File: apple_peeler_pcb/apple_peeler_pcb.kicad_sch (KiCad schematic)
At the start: 14 parts, among them J1 BM03B-SRSS-TB, J2 BM03B-SRSS-TB, SW1 SPST BTN, SW2 SPST BTN, U1 W25Q16JVSS, U2 RP2040, Y1 12MHz

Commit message: use wleds instead of individual leds
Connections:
- net UI/GREEN_LED renamed UI/WLED
- net UI/RED_LED: no longer names the net of U2.7 (GPIO5)
- net UI/YELLOW_LED: no longer names the net of U2.8 (GPIO6)
- no-connect marks 8 -> 10
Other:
- sheet UI ports: added WLED; removed GREEN_LED, RED_LED, YELLOW_LED
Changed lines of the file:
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@@
 	)
 	(no_connect
+		(at 168.91 88.9)
+	)
+	(no_connect
+		(at 168.91 91.44)
+	)
+	(no_connect
 		(at 168.91 144.78)
 	)
@@
 	(wire
 		(pts
-			(xy 168.91 91.44) (xy 181.61 91.44)
-		)
-		(stroke
-			(width 0)
-			(type default)
-		)
-	)
-	(wire
-		(pts
 			(xy 80.01 96.52) (xy 101.6 96.52)
 		)
@@
 	(wire
 		(pts
-			(xy 168.91 88.9) (xy 181.61 88.9)
-		)
-		(stroke
-			(width 0)
-			(type default)
-		)
-	)
-	(wire
-		(pts
 			(xy 87.63 91.44) (xy 87.63 93.98)
 		)
@@
 	(sheet
 		(at 181.61 82.55)
-		(size 17.78 10.16)
+		(size 17.78 5.08)
 		(exclude_from_sim no)
 		(in_bom yes)
@@
 		)
 		(property "Sheetfile" "ui.kicad_sch"
-			(at 181.61 93.2946 0)
+			(at 181.61 88.2146 0)
 			(effects
 				(font
@@
 			)
 		)
-		(pin "GREEN_LED" input
-			(at 181.61 86.36 180)
-			(effects
-				(font
-					(size 1.27 1.27)
-				)
-				(justify left)
-			)
-		)
-		(pin "RED_LED" input
-			(at 181.61 88.9 180)
-			(effects
-				(font
-					(size 1.27 1.27)
-				)
-				(justify left)
-			)
-		)
 		(pin "USR_BTN" output
 			(at 181.61 83.82 180)
@@
 			)
 		)
-		(pin "YELLOW_LED" input
-			(at 181.61 91.44 180)
+		(pin "WLED" input
+			(at 181.61 86.36 180)
 			(effects
 				(font

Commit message: some progress
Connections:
- net USB/DM renamed USB/DN
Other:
- sheet USB ports: added DN; removed DM
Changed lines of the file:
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@@
 			)
 		)
-		(pin "DM" bidirectional
+		(pin "DN" bidirectional
 			(at 115.57 86.36 0)
 			(effects

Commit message: rg | xargs sed goes brrr
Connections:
- net HDMI passthrough/CEC_SINK_MON renamed HDMI passthrough/CEC_B_MON
- net HDMI passthrough/CEC_SINK_PULLDOWN renamed HDMI passthrough/CEC_B_PULLDOWN
- net HDMI passthrough/CEC_SRC_MON renamed HDMI passthrough/CEC_A_MON
- net HDMI passthrough/CEC_SRC_PULLDOWN renamed HDMI passthrough/CEC_A_PULLDOWN
- net HDMI passthrough/HPD_SINK_ASSERT renamed HDMI passthrough/HPD_B_ASSERT
- net HDMI passthrough/HPD_SINK_MON renamed HDMI passthrough/HPD_B_MON
- net HDMI passthrough/HPD_SRC_ASSERT renamed HDMI passthrough/HPD_A_ASSERT
- net HDMI passthrough/HPD_SRC_MON renamed HDMI passthrough/HPD_A_MON
- net HDMI passthrough/SCL_SINK_3V3 renamed HDMI passthrough/SCL_B_3V3
- net HDMI passthrough/SCL_SRC_3V3 renamed HDMI passthrough/SCL_A_3V3
- net HDMI passthrough/SDA_SINK_3V3 renamed HDMI passthrough/SDA_B_3V3
- net HDMI passthrough/SDA_SRC_3V3 renamed HDMI passthrough/SDA_A_3V3
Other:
- sheet HDMI passthrough ports: added CEC_A_MON, CEC_A_PULLDOWN, CEC_B_MON, CEC_B_PULLDOWN, HPD_A_ASSERT, HPD_A_MON, HPD_B_ASSERT, HPD_B_MON, SCL_A_3V3, SCL_B_3V3, SDA_A_3V3, SDA_B_3V3; removed CEC_SINK_MON, CEC_SINK_PULLDOWN, CEC_SRC_MON, CEC_SRC_PULLDOWN, HPD_SINK_ASSERT, HPD_SINK_MON, HPD_SRC_ASSERT, HPD_SRC_MON, SCL_SINK_3V3, SCL_SRC_3V3, SDA_SINK_3V3, SDA_SRC_3V3
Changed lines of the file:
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@@
 			)
 		)
-		(pin "HPD_SINK_MON" output
+		(pin "HPD_B_MON" output
 			(at 228.6 121.92 180)
 			(effects
@@
 			)
 		)
-		(pin "HPD_SRC_ASSERT" input
+		(pin "HPD_A_ASSERT" input
 			(at 228.6 119.38 180)
 			(effects
@@
 			)
 		)
-		(pin "SCL_SINK_3V3" bidirectional
+		(pin "SCL_B_3V3" bidirectional
 			(at 228.6 109.22 180)
 			(effects
@@
 			)
 		)
-		(pin "SCL_SRC_3V3" bidirectional
+		(pin "SCL_A_3V3" bidirectional
 			(at 228.6 104.14 180)
 			(effects
@@
 			)
 		)
-		(pin "SDA_SINK_3V3" bidirectional
+		(pin "SDA_B_3V3" bidirectional
 			(at 228.6 106.68 180)
 			(effects
@@
 			)
 		)
-		(pin "SDA_SRC_3V3" bidirectional
+		(pin "SDA_A_3V3" bidirectional
 			(at 228.6 101.6 180)
 			(effects
@@
 			)
 		)
-		(pin "CEC_SINK_MON" output
+		(pin "CEC_B_MON" output
 			(at 228.6 129.54 180)
 			(effects
@@
 			)
 		)
-		(pin "CEC_SINK_PULLDOWN" input
+		(pin "CEC_B_PULLDOWN" input
 			(at 228.6 132.08 180)
 			(effects
@@
 			)
 		)
-		(pin "CEC_SRC_MON" output
+		(pin "CEC_A_MON" output
 			(at 228.6 137.16 180)
 			(effects
@@
 			)
 		)
-		(pin "CEC_SRC_PULLDOWN" input
+		(pin "CEC_A_PULLDOWN" input
 			(at 228.6 134.62 180)
 			(effects
@@
 			)
 		)
-		(pin "HPD_SINK_ASSERT" input
+		(pin "HPD_B_ASSERT" input
 			(at 228.6 124.46 180)
 			(effects
@@
 			)
 		)
-		(pin "HPD_SRC_MON" output
+		(pin "HPD_A_MON" output
 			(at 228.6 116.84 180)
 			(effects

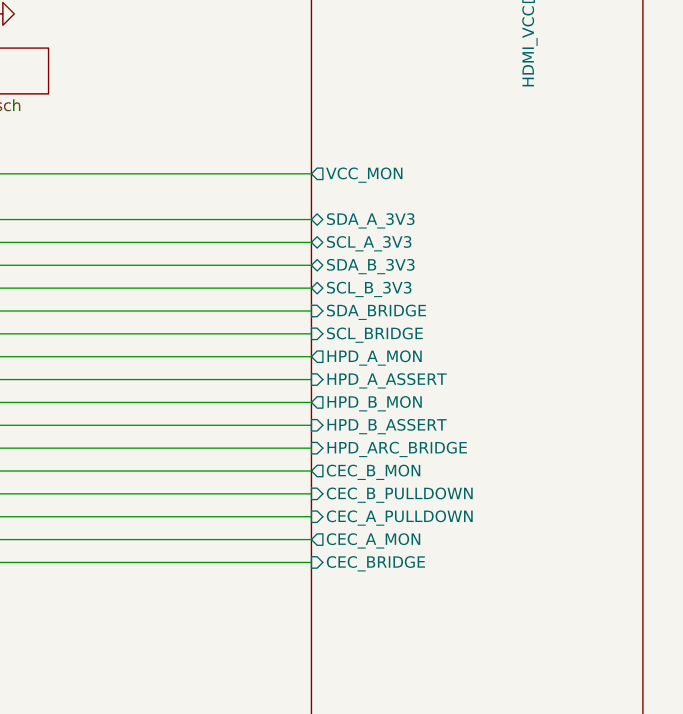
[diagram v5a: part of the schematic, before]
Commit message: route all the rp2040 pins
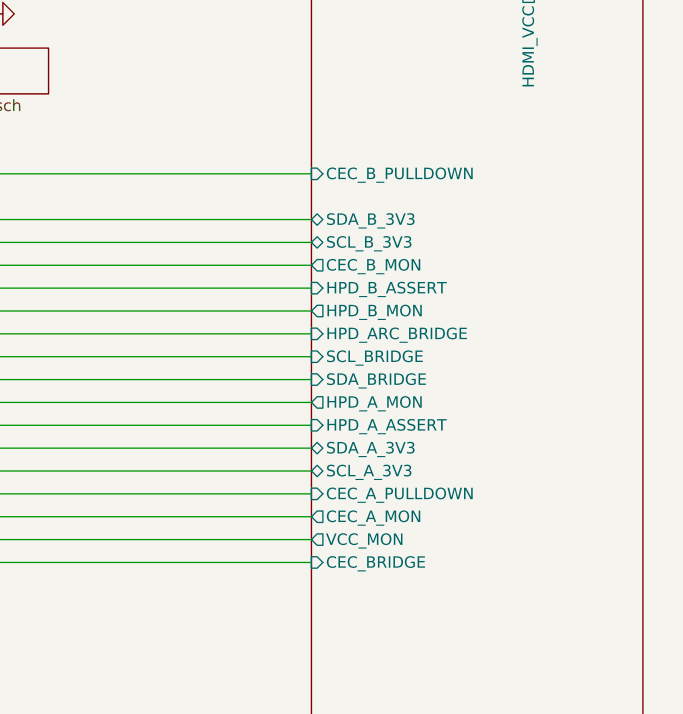
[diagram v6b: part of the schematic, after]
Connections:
- net HDMI passthrough/CEC_A_MON: now also U2.35 (GPIO23); no longer U2.36 (GPIO24)
- net HDMI passthrough/CEC_A_PULLDOWN: now also U2.34 (GPIO22); no longer U2.35 (GPIO23)
- net HDMI passthrough/CEC_B_MON: now also U2.15 (GPIO12); no longer U2.32 (GPIO21)
- net HDMI passthrough/CEC_B_PULLDOWN: now also U2.11 (GPIO8); no longer U2.34 (GPIO22)
- net HDMI passthrough/HPD_ARC_BRIDGE: now also U2.18 (GPIO15); no longer U2.31 (GPIO20)
- net HDMI passthrough/HPD_A_ASSERT: now also U2.30 (GPIO19); no longer U2.28 (GPIO17)
- net HDMI passthrough/HPD_A_MON: now also U2.29 (GPIO18); no longer U2.27 (GPIO16)
- net HDMI passthrough/HPD_B_ASSERT: now also U2.16 (GPIO13); no longer U2.30 (GPIO19)
- net HDMI passthrough/HPD_B_MON: now also U2.17 (GPIO14); no longer U2.29 (GPIO18)
- net HDMI passthrough/SCL_A_3V3: now also U2.32 (GPIO21); no longer U2.14 (GPIO11)
- net HDMI passthrough/SCL_BRIDGE: now also U2.27 (GPIO16); no longer U2.18 (GPIO15)
- net HDMI passthrough/SCL_B_3V3: now also U2.14 (GPIO11); no longer U2.16 (GPIO13)
- net HDMI passthrough/SDA_A_3V3: now also U2.31 (GPIO20); no longer U2.13 (GPIO10)
- net HDMI passthrough/SDA_BRIDGE: now also U2.28 (GPIO17); no longer U2.17 (GPIO14)
- net HDMI passthrough/SDA_B_3V3: now also U2.13 (GPIO10); no longer U2.15 (GPIO12)
- net HDMI passthrough/VCC_MON: now also U2.36 (GPIO24); no longer U2.11 (GPIO8)
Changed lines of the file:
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@@
 		)
 		(pin "HPD_ARC_BRIDGE" input
+			(at 228.6 114.3 180)
+			(effects
+				(font
+					(size 1.27 1.27)
+				)
+				(justify left)
+			)
+		)
+		(pin "HPD_B_MON" output
+			(at 228.6 111.76 180)
+			(effects
+				(font
+					(size 1.27 1.27)
+				)
+				(justify left)
+			)
+		)
+		(pin "HPD_A_ASSERT" input
+			(at 228.6 124.46 180)
+			(effects
+				(font
+					(size 1.27 1.27)
+				)
+				(justify left)
+			)
+		)
+		(pin "SCL_BRIDGE" input
+			(at 228.6 116.84 180)
+			(effects
+				(font
+					(size 1.27 1.27)
+				)
+				(justify left)
+			)
+		)
+		(pin "SCL_B_3V3" bidirectional
+			(at 228.6 104.14 180)
+			(effects
+				(font
+					(size 1.27 1.27)
+				)
+				(justify left)
+			)
+		)
+		(pin "SCL_A_3V3" bidirectional
+			(at 228.6 129.54 180)
+			(effects
+				(font
+					(size 1.27 1.27)
+				)
+				(justify left)
+			)
+		)
+		(pin "SDA_BRIDGE" input
+			(at 228.6 119.38 180)
+			(effects
+				(font
+					(size 1.27 1.27)
+				)
+				(justify left)
+			)
+		)
+		(pin "SDA_B_3V3" bidirectional
+			(at 228.6 101.6 180)
+			(effects
+				(font
+					(size 1.27 1.27)
+				)
+				(justify left)
+			)
+		)
+		(pin "SDA_A_3V3" bidirectional
 			(at 228.6 127 180)
 			(effects
@@
 			)
 		)
-		(pin "HPD_B_MON" output
-			(at 228.6 121.92 180)
+		(pin "VCC_MON" output
+			(at 228.6 137.16 180)
 			(effects
 				(font
@@
 			)
 		)
-		(pin "HPD_A_ASSERT" input
-			(at 228.6 119.38 180)
+		(pin "CEC_B_MON" output
+			(at 228.6 106.68 180)
 			(effects
 				(font
@@
 			)
 		)
-		(pin "SCL_BRIDGE" input
-			(at 228.6 114.3 180)
+		(pin "CEC_B_PULLDOWN" input
+			(at 228.6 96.52 180)
 			(effects
 				(font
@@
 			)
 		)
-		(pin "SCL_B_3V3" bidirectional
+		(pin "CEC_A_MON" output
+			(at 228.6 134.62 180)
+			(effects
+				(font
+					(size 1.27 1.27)
+				)
+				(justify left)
+			)
+		)
+		(pin "CEC_A_PULLDOWN" input
+			(at 228.6 132.08 180)
+			(effects
+				(font
+					(size 1.27 1.27)
+				)
+				(justify left)
+			)
+		)
+		(pin "HPD_B_ASSERT" input
 			(at 228.6 109.22 180)
 			(effects
@@
 			)
 		)
-		(pin "SCL_A_3V3" bidirectional
-			(at 228.6 104.14 180)
+		(pin "HPD_A_MON" output
+			(at 228.6 121.92 180)
 			(effects
 				(font
-					(size 1.27 1.27)
-				)
-				(justify left)
-			)
-		)
-		(pin "SDA_BRIDGE" input
-			(at 228.6 111.76 180)
-			(effects
-				(font
-					(size 1.27 1.27)
-				)
-				(justify left)
-			)
-		)
-		(pin "SDA_B_3V3" bidirectional
-			(at 228.6 106.68 180)
-			(effects
-				(font
-					(size 1.27 1.27)
-				)
-				(justify left)
-			)
-		)
-		(pin "SDA_A_3V3" bidirectional
-			(at 228.6 101.6 180)
-			(effects
-				(font
-					(size 1.27 1.27)
-				)
-				(justify left)
-			)
-		)
-		(pin "VCC_MON" output
-			(at 228.6 96.52 180)
-			(effects
-				(font
-					(size 1.27 1.27)
-				)
-				(justify left)
-			)
-		)
-		(pin "CEC_B_MON" output
-			(at 228.6 129.54 180)
-			(effects
-				(font
-					(size 1.27 1.27)
-				)
-				(justify left)
-			)
-		)
-		(pin "CEC_B_PULLDOWN" input
-			(at 228.6 132.08 180)
-			(effects
-				(font
-					(size 1.27 1.27)
-				)
-				(justify left)
-			)
-		)
-		(pin "CEC_A_MON" output
-			(at 228.6 137.16 180)
-			(effects
-				(font
-					(size 1.27 1.27)
-				)
-				(justify left)
-			)
-		)
-		(pin "CEC_A_PULLDOWN" input
-			(at 228.6 134.62 180)
-			(effects
-				(font
-					(size 1.27 1.27)
-				)
-				(justify left)
-			)
-		)
-		(pin "HPD_B_ASSERT" input
-			(at 228.6 124.46 180)
-			(effects
-				(font
-					(size 1.27 1.27)
-				)
-				(justify left)
-			)
-		)
-		(pin "HPD_A_MON" output
-			(at 228.6 116.84 180)
-			(effects
-				(font

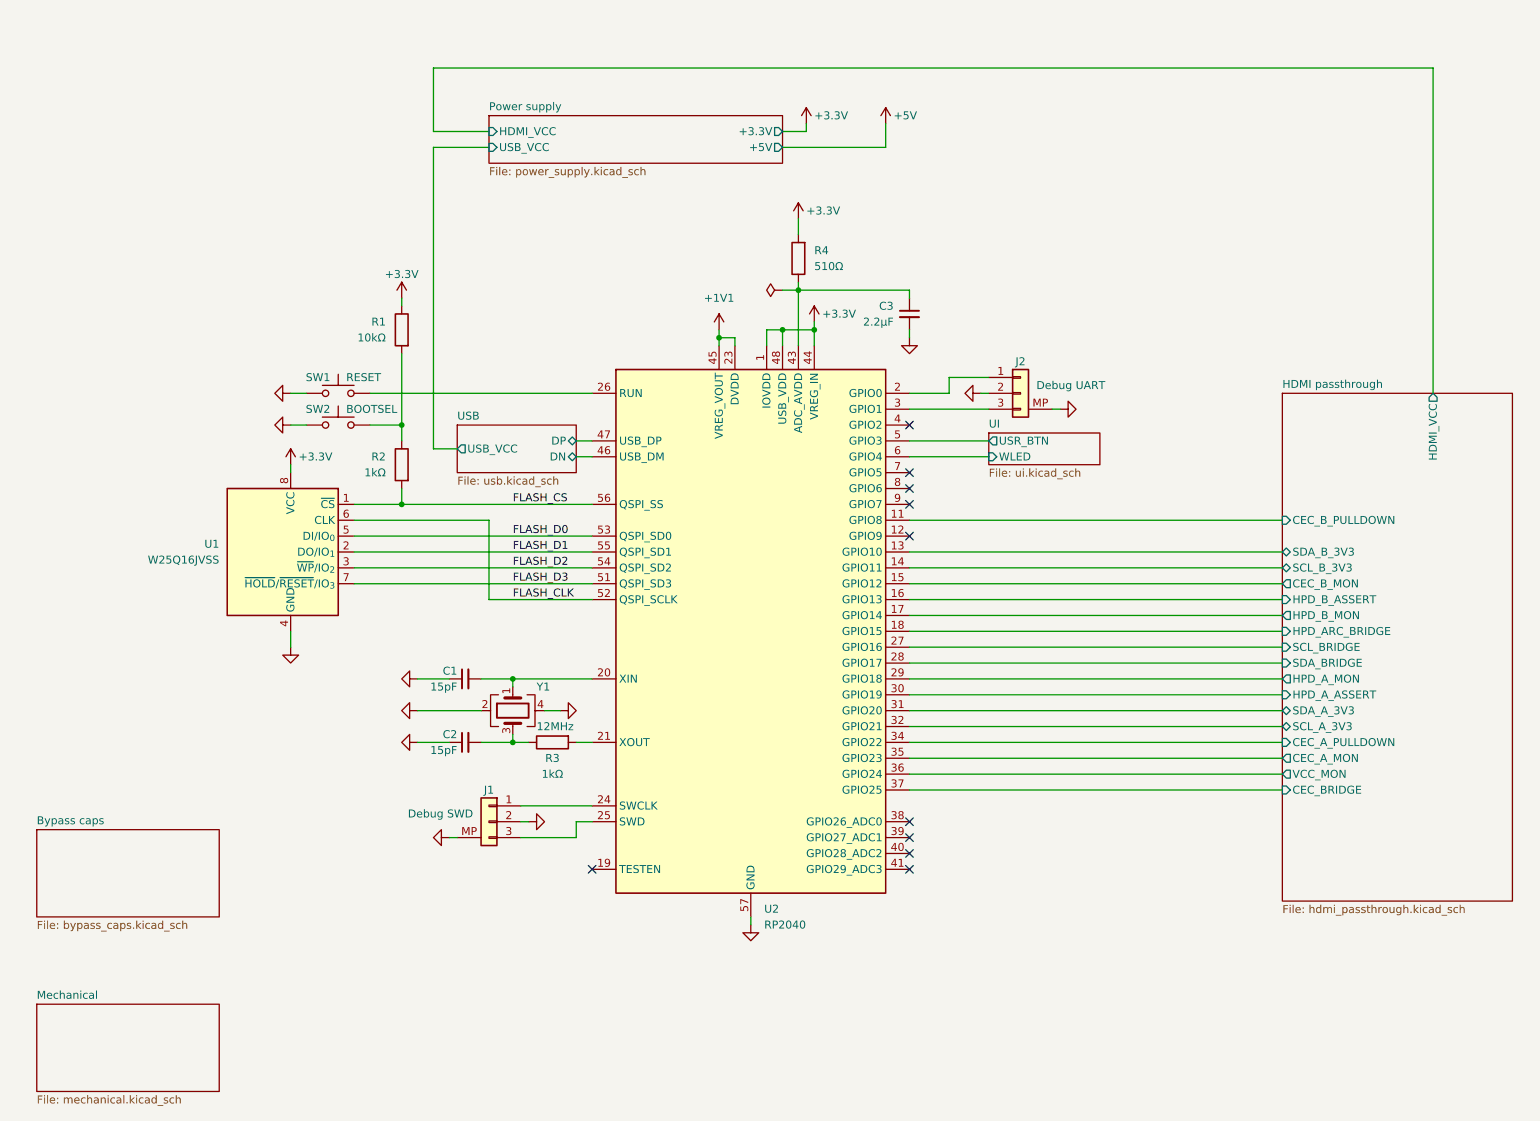
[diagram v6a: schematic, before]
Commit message: replace fancy debug connectors by pin header to save $8
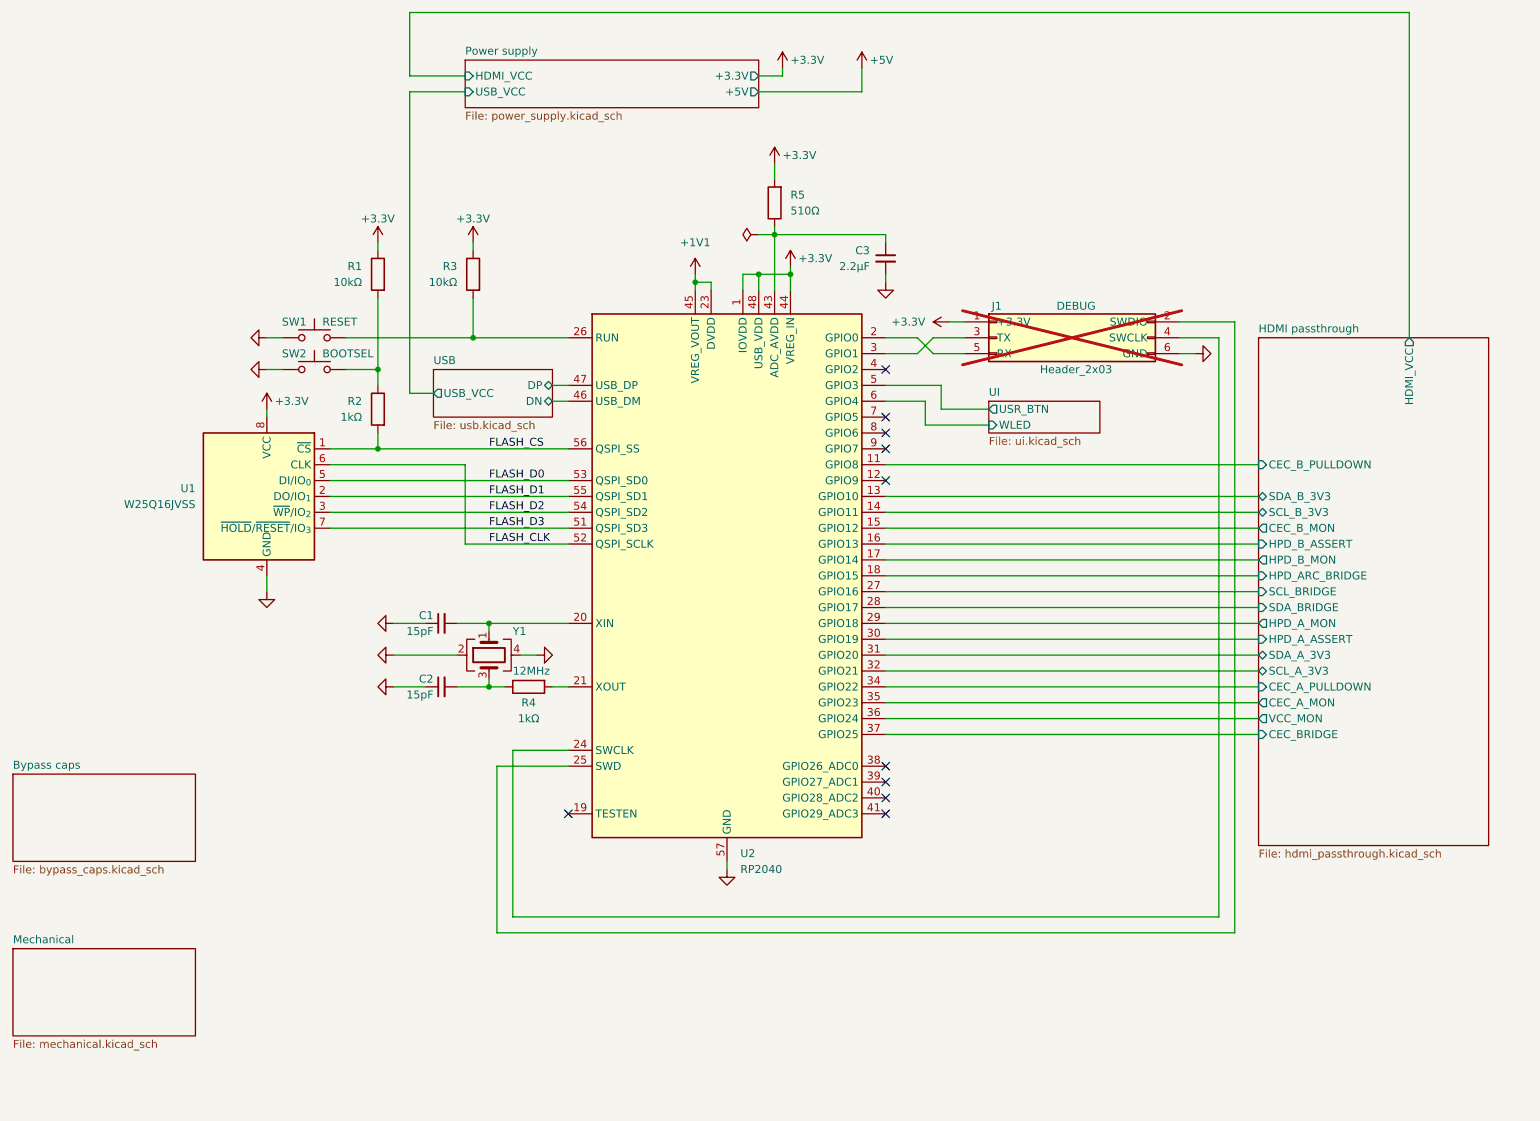
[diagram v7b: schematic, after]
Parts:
- removed J1, J2: BM03B-SRSS-TB, Connector_JST:JST_SH_BM03B-SRSS-TB_1x03-1MP_P1.00mm_Vertical, symbol conn:Conn_01x03
- added J1: Header_2x03, conn:PinHeader_2x03_P2.54mm_Vertical, symbol conn:Conn_02x03_Odd_Even
- added R3: 10kΩ, Resistor_SMD:R_0805_2012Metric, symbol Device:R
- renumbered R3 to R4, R4 to R5
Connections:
- net +3.3V: now also J1.1 (Pin_1), R3.1
- net GND: now also J1.6 (Pin_6)
- net at SW1.2, U2.26 (RUN): now also R3.2
- net at U2.2 (GPIO0): now also J1.5 (Pin_5)
- net at U2.3 (GPIO1): now also J1.3 (Pin_3)
- net at U2.24 (SWCLK): now also J1.4 (Pin_4)
- net at U2.25 (SWD): now also J1.2 (Pin_2)
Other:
- moved on the sheet: C1, C2, C3, R1, R2, R4, R5, SW1, SW2, U1, U2, Y1

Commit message: add comment
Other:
- note added: "NOTE: GPIO24 is used by the bootloader for VBUS detection, but I am too lazy to connect that so use the bootloader only with HDMI disconnected"
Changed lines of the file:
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@@
 	(generator_version "9.0")
 	(paper "A4")
+	(text "NOTE: GPIO24 is used by\nthe bootloader for VBUS\ndetection, but I am too\nlazy to connect that\nso use the bootloader only\nwith HDMI disconnected"
+		(exclude_from_sim no)
+		(at 175.26 139.7 0)
+		(effects
+			(font
+				(size 1.27 1.27)
+			)
+			(justify left)
+		)
+	)
 	(junction
 		(at 83.82 85.09)
